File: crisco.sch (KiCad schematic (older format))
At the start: 43 parts, among them J1 LED, J2 OLED, U1 ProMicro

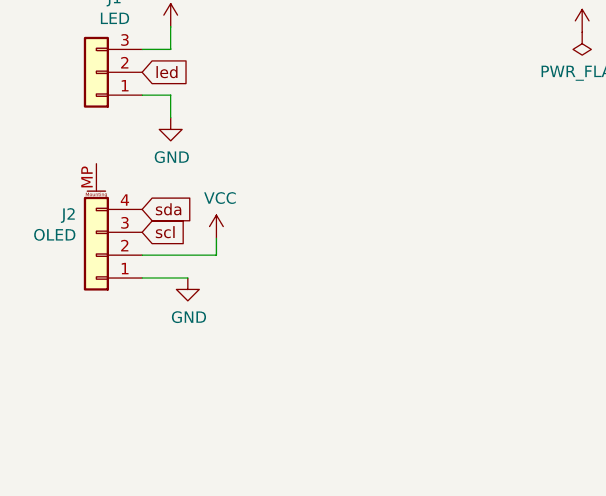
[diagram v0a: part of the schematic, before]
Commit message: added pullup resistors, bom, and instructions
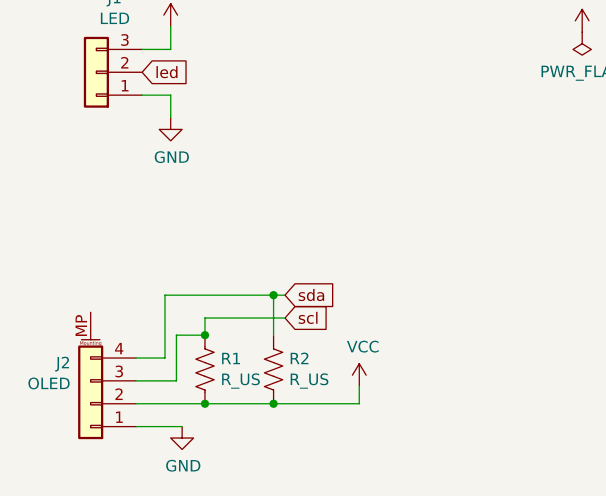
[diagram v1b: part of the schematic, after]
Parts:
- added R1, R2: R_US, Resistor_THT:R_Axial_DIN0204_L3.6mm_D1.6mm_P5.08mm_Horizontal, symbol Device:R_US
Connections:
- net VCC: now also R1.2, R2.2
- net scl: now also R1.1
- net sda: now also R2.1
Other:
- moved on the sheet: J2
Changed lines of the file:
@@
 L Connector_Generic_MountingPin:Conn_01x04_MountingPin J2
 U 1 1 61CC6089
-P 1975 4600
-F 0 "J2" H 2063 4422 50  0000 L CNN
-F 1 "OLED" H 2063 4513 50  0000 L CNN
-F 2 "Connector_PinHeader_2.54mm:PinHeader_1x04_P2.54mm_Vertical" H 1975 4600 50  0001 C CNN
-F 3 "~" H 1975 4600 50  0001 C CNN
-	1    1975 4600
+P 1950 5250
+F 0 "J2" H 2038 5072 50  0000 L CNN
+F 1 "OLED" H 2038 5163 50  0000 L CNN
+F 2 "Connector_PinHeader_2.54mm:PinHeader_1x04_P2.54mm_Vertical" H 1950 5250 50  0001 C CNN
+F 3 "~" H 1950 5250 50  0001 C CNN
+	1    1950 5250
 	-1   0    0    1
 $EndComp
@@
 L power:VCC #PWR0109
 U 1 1 61CCE8B0
-P 2500 4525
-F 0 "#PWR0109" H 2500 4375 50  0001 C CNN
-F 1 "VCC" H 2517 4698 50  0000 C CNN
-F 2 "" H 2500 4525 50  0001 C CNN
-F 3 "" H 2500 4525 50  0001 C CNN
-	1    2500 4525
+P 3125 5175
+F 0 "#PWR0109" H 3125 5025 50  0001 C CNN
+F 1 "VCC" H 3142 5348 50  0000 C CNN
+F 2 "" H 3125 5175 50  0001 C CNN
+F 3 "" H 3125 5175 50  0001 C CNN
+	1    3125 5175
 	1    0    0    -1
 $EndComp
@@
 L power:GND #PWR0110
 U 1 1 61CD2B6D
-P 2375 4700
-F 0 "#PWR0110" H 2375 4450 50  0001 C CNN
-F 1 "GND" H 2380 4527 50  0000 C CNN
-F 2 "" H 2375 4700 50  0001 C CNN
-F 3 "" H 2375 4700 50  0001 C CNN
-	1    2375 4700
+P 2350 5350
+F 0 "#PWR0110" H 2350 5100 50  0001 C CNN
+F 1 "GND" H 2355 5177 50  0000 C CNN
+F 2 "" H 2350 5350 50  0001 C CNN
+F 3 "" H 2350 5350 50  0001 C CNN
+	1    2350 5350
 	1    0    0    -1
 $EndComp
-Text GLabel 2175 4500 2    50   Input ~ 0
+Text GLabel 2800 4875 2    50   Input ~ 0
 scl
-Text GLabel 2175 4400 2    50   Input ~ 0
+Text GLabel 2800 4775 2    50   Input ~ 0
 sda
 Wire Wire Line
-	2175 4600 2500 4600
+	3125 5250 3125 5175
 Wire Wire Line
-	2500 4600 2500 4525
+	2150 5350 2350 5350
+NoConn ~ 3650 2200
+$Comp
+L Device:R_US R1
+U 1 1 61D4AEF9
+P 2450 5100
+F 0 "R1" H 2518 5146 50  0000 L CNN
+F 1 "R_US" H 2518 5055 50  0000 L CNN
+F 2 "Resistor_THT:R_Axial_DIN0204_L3.6mm_D1.6mm_P5.08mm_Horizontal" V 2490 5090 50  0001 C CNN
+F 3 "~" H 2450 5100 50  0001 C CNN
+	1    2450 5100
+	1    0    0    -1
+$EndComp
+$Comp
+L Device:R_US R2
+U 1 1 61D4BA80
+P 2750 5100
+F 0 "R2" H 2818 5146 50  0000 L CNN
+F 1 "R_US" H 2818 5055 50  0000 L CNN
+F 2 "Resistor_THT:R_Axial_DIN0204_L3.6mm_D1.6mm_P5.08mm_Horizontal" V 2790 5090 50  0001 C CNN
+F 3 "~" H 2750 5100 50  0001 C CNN
+	1    2750 5100
+	1    0    0    -1
+$EndComp
 Wire Wire Line
-	2175 4700 2375 4700
-NoConn ~ 3650 2200
+	2750 5250 3125 5250
+Wire Wire Line
+	2750 5250 2450 5250
+Connection ~ 2750 5250
+Wire Wire Line
+	2450 5250 2150 5250
+Connection ~ 2450 5250
+Wire Wire Line
+	2325 5150 2150 5150
+Wire Wire Line
+	2275 5050 2275 4775
+Wire Wire Line
+	2275 4775 2750 4775
+Wire Wire Line
+	2325 4950 2450 4950
+Wire Wire Line
+	2450 4950 2450 4875
+Wire Wire Line
+	2450 4875 2800 4875
+Wire Wire Line
+	2325 4950 2325 5150
+Connection ~ 2450 4950
+Wire Wire Line
+	2750 4775 2750 4950
+Connection ~ 2750 4775
+Wire Wire Line
+	2750 4775 2800 4775
+Wire Wire Line
+	2150 5050 2275 5050
 $EndSCHEMATC

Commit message: update gerber
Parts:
- removed R1, R2: R_US, Resistor_THT:R_Axial_DIN0204_L3.6mm_D1.6mm_P5.08mm_Horizontal, symbol Device:R_US
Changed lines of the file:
@@
 L power:VCC #PWR0109
 U 1 1 61CCE8B0
-P 3125 5175
-F 0 "#PWR0109" H 3125 5025 50  0001 C CNN
-F 1 "VCC" H 3142 5348 50  0000 C CNN
-F 2 "" H 3125 5175 50  0001 C CNN
-F 3 "" H 3125 5175 50  0001 C CNN
-	1    3125 5175
+P 2625 5175
+F 0 "#PWR0109" H 2625 5025 50  0001 C CNN
+F 1 "VCC" H 2642 5348 50  0000 C CNN
+F 2 "" H 2625 5175 50  0001 C CNN
+F 3 "" H 2625 5175 50  0001 C CNN
+	1    2625 5175
 	1    0    0    -1
 $EndComp
@@
 	1    0    0    -1
 $EndComp
-Text GLabel 2800 4875 2    50   Input ~ 0
+Text GLabel 2150 5150 2    50   Input ~ 0
 scl
-Text GLabel 2800 4775 2    50   Input ~ 0
+Text GLabel 2150 5050 2    50   Input ~ 0
 sda
 Wire Wire Line
-	3125 5250 3125 5175
+	2625 5250 2625 5175
 Wire Wire Line
 	2150 5350 2350 5350
 NoConn ~ 3650 2200
-$Comp
-L Device:R_US R1
-U 1 1 61D4AEF9
-P 2450 5100
-F 0 "R1" H 2518 5146 50  0000 L CNN
-F 1 "R_US" H 2518 5055 50  0000 L CNN
-F 2 "Resistor_THT:R_Axial_DIN0204_L3.6mm_D1.6mm_P5.08mm_Horizontal" V 2490 5090 50  0001 C CNN
-F 3 "~" H 2450 5100 50  0001 C CNN
-	1    2450 5100
-	1    0    0    -1
-$EndComp
-$Comp
-L Device:R_US R2
-U 1 1 61D4BA80
-P 2750 5100
-F 0 "R2" H 2818 5146 50  0000 L CNN
-F 1 "R_US" H 2818 5055 50  0000 L CNN
-F 2 "Resistor_THT:R_Axial_DIN0204_L3.6mm_D1.6mm_P5.08mm_Horizontal" V 2790 5090 50  0001 C CNN
-F 3 "~" H 2750 5100 50  0001 C CNN
-	1    2750 5100
-	1    0    0    -1
-$EndComp
 Wire Wire Line
-	2750 5250 3125 5250
-Wire Wire Line
-	2750 5250 2450 5250
-Connection ~ 2750 5250
-Wire Wire Line
-	2450 5250 2150 5250
-Connection ~ 2450 5250
-Wire Wire Line
-	2325 5150 2150 5150
-Wire Wire Line
-	2275 5050 2275 4775
-Wire Wire Line
-	2275 4775 2750 4775
-Wire Wire Line
-	2325 4950 2450 4950
-Wire Wire Line
-	2450 4950 2450 4875
-Wire Wire Line
-	2450 4875 2800 4875
-Wire Wire Line
-	2325 4950 2325 5150
-Connection ~ 2450 4950
-Wire Wire Line
-	2750 4775 2750 4950
-Connection ~ 2750 4775
-Wire Wire Line
-	2750 4775 2800 4775
-Wire Wire Line
-	2150 5050 2275 5050
+	2150 5250 2625 5250
 $EndSCHEMATC

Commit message: reset switch
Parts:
- added SW1: SW_Push, Button_Switch_SMD:SW_SPST_B3U-1000P, symbol Switch:SW_Push
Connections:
- net GND: now also SW1.2
- net rst: now reaches U1.22 (RST)
- net rst: now also SW1.1
- no-connect marks 45 -> 44
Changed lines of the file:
@@
 Wire Wire Line
 	2150 5350 2350 5350
-NoConn ~ 3650 2200
 Wire Wire Line
 	2150 5250 2625 5250
+Text GLabel 3650 2200 2    50   Input ~ 0
+rst
+$Comp
+L Switch:SW_Push SW1
+U 1 1 61D5D662
+P 3175 3875
+F 0 "SW1" H 3175 4160 50  0000 C CNN
+F 1 "SW_Push" H 3175 4069 50  0000 C CNN
+F 2 "Button_Switch_SMD:SW_SPST_B3U-1000P" H 3175 4075 50  0001 C CNN
+F 3 "~" H 3175 4075 50  0001 C CNN
+	1    3175 3875
+	1    0    0    -1
+$EndComp
+Text GLabel 2975 3875 0    50   Input ~ 0
+rst
+$Comp
+L power:GND #PWR0106
+U 1 1 61D6114F
+P 3375 3875
+F 0 "#PWR0106" H 3375 3625 50  0001 C CNN
+F 1 "GND" H 3380 3702 50  0000 C CNN
+F 2 "" H 3375 3875 50  0001 C CNN
+F 3 "" H 3375 3875 50  0001 C CNN
+	1    3375 3875
+	1    0    0    -1
+$EndComp
 $EndSCHEMATC

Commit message: mx/alps hybrid version
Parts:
- MX1, MX10, MX11, MX12, MX13, MX14, MX15, MX16, MX17, MX18, MX19, MX2, MX20, MX3, MX4, MX5, MX6, MX7, MX8, MX9: footprint MX_Alps_Hybrid:MXOnly-1U-NoLED -> MX_Alps_Hybrid:MX-1U-NoLED
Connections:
- net GND: now also J2.MP (MountPin)
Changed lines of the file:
@@
 F 0 "MX1" H 5036 2217 60  0000 C CNN
 F 1 "MX-1U" H 5036 2143 20  0000 C CNN
-F 2 "MX_Alps_Hybrid:MXOnly-1U-NoLED" H 4925 1975 60  0001 C CNN
+F 2 "MX_Alps_Hybrid:MX-1U-NoLED" H 4925 1975 60  0001 C CNN
 F 3 "" H 4925 1975 60  0001 C CNN
 	1    4950 2000
@@
 F 0 "MX2" H 5636 2217 60  0000 C CNN
 F 1 "MX-1U" H 5636 2143 20  0000 C CNN
-F 2 "MX_Alps_Hybrid:MXOnly-1U-NoLED" H 5525 1975 60  0001 C CNN
+F 2 "MX_Alps_Hybrid:MX-1U-NoLED" H 5525 1975 60  0001 C CNN
 F 3 "" H 5525 1975 60  0001 C CNN
 	1    5550 2000
@@
 F 0 "MX3" H 6236 2217 60  0000 C CNN
 F 1 "MX-1U" H 6236 2143 20  0000 C CNN
-F 2 "MX_Alps_Hybrid:MXOnly-1U-NoLED" H 6125 1975 60  0001 C CNN
+F 2 "MX_Alps_Hybrid:MX-1U-NoLED" H 6125 1975 60  0001 C CNN
 F 3 "" H 6125 1975 60  0001 C CNN
 	1    6150 2000
@@
 F 0 "MX11" H 5036 2967 60  0000 C CNN
 F 1 "MX-1U" H 5036 2893 20  0000 C CNN
-F 2 "MX_Alps_Hybrid:MXOnly-1U-NoLED" H 4925 2725 60  0001 C CNN
+F 2 "MX_Alps_Hybrid:MX-1U-NoLED" H 4925 2725 60  0001 C CNN
 F 3 "" H 4925 2725 60  0001 C CNN
 	1    4950 2750
@@
 F 0 "MX12" H 5636 2967 60  0000 C CNN
 F 1 "MX-1U" H 5636 2893 20  0000 C CNN
-F 2 "MX_Alps_Hybrid:MXOnly-1U-NoLED" H 5525 2725 60  0001 C CNN
+F 2 "MX_Alps_Hybrid:MX-1U-NoLED" H 5525 2725 60  0001 C CNN
 F 3 "" H 5525 2725 60  0001 C CNN
 	1    5550 2750
@@
 F 0 "MX13" H 6236 2967 60  0000 C CNN
 F 1 "MX-1U" H 6236 2893 20  0000 C CNN
-F 2 "MX_Alps_Hybrid:MXOnly-1U-NoLED" H 6125 2725 60  0001 C CNN
+F 2 "MX_Alps_Hybrid:MX-1U-NoLED" H 6125 2725 60  0001 C CNN
 F 3 "" H 6125 2725 60  0001 C CNN
 	1    6150 2750
@@
 F 0 "MX4" H 6836 2217 60  0000 C CNN
 F 1 "MX-1U" H 6836 2143 20  0000 C CNN
-F 2 "MX_Alps_Hybrid:MXOnly-1U-NoLED" H 6725 1975 60  0001 C CNN
+F 2 "MX_Alps_Hybrid:MX-1U-NoLED" H 6725 1975 60  0001 C CNN
 F 3 "" H 6725 1975 60  0001 C CNN
 	1    6750 2000
@@
 F 0 "MX14" H 6836 2967 60  0000 C CNN
 F 1 "MX-1U" H 6836 2893 20  0000 C CNN
-F 2 "MX_Alps_Hybrid:MXOnly-1U-NoLED" H 6725 2725 60  0001 C CNN
+F 2 "MX_Alps_Hybrid:MX-1U-NoLED" H 6725 2725 60  0001 C CNN
 F 3 "" H 6725 2725 60  0001 C CNN
 	1    6750 2750
@@
 F 0 "MX5" H 7436 2217 60  0000 C CNN
 F 1 "MX-1U" H 7436 2143 20  0000 C CNN
-F 2 "MX_Alps_Hybrid:MXOnly-1U-NoLED" H 7325 1975 60  0001 C CNN
+F 2 "MX_Alps_Hybrid:MX-1U-NoLED" H 7325 1975 60  0001 C CNN
 F 3 "" H 7325 1975 60  0001 C CNN
 	1    7350 2000
@@
 F 0 "MX15" H 7436 2967 60  0000 C CNN
 F 1 "MX-1U" H 7436 2893 20  0000 C CNN
-F 2 "MX_Alps_Hybrid:MXOnly-1U-NoLED" H 7325 2725 60  0001 C CNN
+F 2 "MX_Alps_Hybrid:MX-1U-NoLED" H 7325 2725 60  0001 C CNN
 F 3 "" H 7325 2725 60  0001 C CNN
 	1    7350 2750
@@
 F 0 "MX6" H 8036 2217 60  0000 C CNN
 F 1 "MX-1U" H 8036 2143 20  0000 C CNN
-F 2 "MX_Alps_Hybrid:MXOnly-1U-NoLED" H 7925 1975 60  0001 C CNN
+F 2 "MX_Alps_Hybrid:MX-1U-NoLED" H 7925 1975 60  0001 C CNN
 F 3 "" H 7925 1975 60  0001 C CNN
 	1    7950 2000
@@
 F 0 "MX16" H 8036 2967 60  0000 C CNN
 F 1 "MX-1U" H 8036 2893 20  0000 C CNN
-F 2 "MX_Alps_Hybrid:MXOnly-1U-NoLED" H 7925 2725 60  0001 C CNN
+F 2 "MX_Alps_Hybrid:MX-1U-NoLED" H 7925 2725 60  0001 C CNN
 F 3 "" H 7925 2725 60  0001 C CNN
 	1    7950 2750
@@
 F 0 "MX7" H 8636 2217 60  0000 C CNN
 F 1 "MX-1U" H 8636 2143 20  0000 C CNN
-F 2 "MX_Alps_Hybrid:MXOnly-1U-NoLED" H 8525 1975 60  0001 C CNN
+F 2 "MX_Alps_Hybrid:MX-1U-NoLED" H 8525 1975 60  0001 C CNN
 F 3 "" H 8525 1975 60  0001 C CNN
 	1    8550 2000
@@
 F 0 "MX17" H 8636 2967 60  0000 C CNN
 F 1 "MX-1U" H 8636 2893 20  0000 C CNN
-F 2 "MX_Alps_Hybrid:MXOnly-1U-NoLED" H 8525 2725 60  0001 C CNN
+F 2 "MX_Alps_Hybrid:MX-1U-NoLED" H 8525 2725 60  0001 C CNN
 F 3 "" H 8525 2725 60  0001 C CNN
 	1    8550 2750
@@
 F 0 "MX8" H 9236 2217 60  0000 C CNN
 F 1 "MX-1U" H 9236 2143 20  0000 C CNN
-F 2 "MX_Alps_Hybrid:MXOnly-1U-NoLED" H 9125 1975 60  0001 C CNN
+F 2 "MX_Alps_Hybrid:MX-1U-NoLED" H 9125 1975 60  0001 C CNN
 F 3 "" H 9125 1975 60  0001 C CNN
 	1    9150 2000
@@
 F 0 "MX18" H 9236 2967 60  0000 C CNN
 F 1 "MX-1U" H 9236 2893 20  0000 C CNN
-F 2 "MX_Alps_Hybrid:MXOnly-1U-NoLED" H 9125 2725 60  0001 C CNN
+F 2 "MX_Alps_Hybrid:MX-1U-NoLED" H 9125 2725 60  0001 C CNN
 F 3 "" H 9125 2725 60  0001 C CNN
 	1    9150 2750
@@
 F 0 "MX9" H 9836 2217 60  0000 C CNN
 F 1 "MX-1U" H 9836 2143 20  0000 C CNN
-F 2 "MX_Alps_Hybrid:MXOnly-1U-NoLED" H 9725 1975 60  0001 C CNN
+F 2 "MX_Alps_Hybrid:MX-1U-NoLED" H 9725 1975 60  0001 C CNN
 F 3 "" H 9725 1975 60  0001 C CNN
 	1    9750 2000
@@
 F 0 "MX19" H 9836 2967 60  0000 C CNN
 F 1 "MX-1U" H 9836 2893 20  0000 C CNN
-F 2 "MX_Alps_Hybrid:MXOnly-1U-NoLED" H 9725 2725 60  0001 C CNN
+F 2 "MX_Alps_Hybrid:MX-1U-NoLED" H 9725 2725 60  0001 C CNN
 F 3 "" H 9725 2725 60  0001 C CNN
 	1    9750 2750
@@
 F 0 "MX10" H 10436 2217 60  0000 C CNN
 F 1 "MX-1U" H 10436 2143 20  0000 C CNN
-F 2 "MX_Alps_Hybrid:MXOnly-1U-NoLED" H 10325 1975 60  0001 C CNN
+F 2 "MX_Alps_Hybrid:MX-1U-NoLED" H 10325 1975 60  0001 C CNN
 F 3 "" H 10325 1975 60  0001 C CNN
 	1    10350 2000
@@
 F 0 "MX20" H 10436 2967 60  0000 C CNN
 F 1 "MX-1U" H 10436 2893 20  0000 C CNN
-F 2 "MX_Alps_Hybrid:MXOnly-1U-NoLED" H 10325 2725 60  0001 C CNN
+F 2 "MX_Alps_Hybrid:MX-1U-NoLED" H 10325 2725 60  0001 C CNN
 F 3 "" H 10325 2725 60  0001 C CNN
 	1    10350 2750
@@
 	1    0    0    -1
 $EndComp
+$Comp
+L power:GND #PWR0111
+U 1 1 61D60F29
+P 1950 4850
+F 0 "#PWR0111" H 1950 4600 50  0001 C CNN
+F 1 "GND" H 1955 4677 50  0000 C CNN
+F 2 "" H 1950 4850 50  0001 C CNN
+F 3 "" H 1950 4850 50  0001 C CNN
+	1    1950 4850
+	-1   0    0    1
+$EndComp
 $EndSCHEMATC

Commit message: choc hybrid
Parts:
- MX1, MX10, MX11, MX12, MX13, MX14, MX15, MX16, MX17, MX18, MX19, MX2, MX20, MX3, MX4, MX5, MX6, MX7, MX8, MX9: footprint MX_Alps_Hybrid:MX-1U-NoLED -> MX_Alps_Hybrid:MX-Choc-1U-NoLED
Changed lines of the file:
@@
 F 0 "MX1" H 5036 2217 60  0000 C CNN
 F 1 "MX-1U" H 5036 2143 20  0000 C CNN
-F 2 "MX_Alps_Hybrid:MX-1U-NoLED" H 4925 1975 60  0001 C CNN
+F 2 "MX_Alps_Hybrid:MX-Choc-1U-NoLED" H 4925 1975 60  0001 C CNN
 F 3 "" H 4925 1975 60  0001 C CNN
 	1    4950 2000
@@
 F 0 "MX2" H 5636 2217 60  0000 C CNN
 F 1 "MX-1U" H 5636 2143 20  0000 C CNN
-F 2 "MX_Alps_Hybrid:MX-1U-NoLED" H 5525 1975 60  0001 C CNN
+F 2 "MX_Alps_Hybrid:MX-Choc-1U-NoLED" H 5525 1975 60  0001 C CNN
 F 3 "" H 5525 1975 60  0001 C CNN
 	1    5550 2000
@@
 F 0 "MX3" H 6236 2217 60  0000 C CNN
 F 1 "MX-1U" H 6236 2143 20  0000 C CNN
-F 2 "MX_Alps_Hybrid:MX-1U-NoLED" H 6125 1975 60  0001 C CNN
+F 2 "MX_Alps_Hybrid:MX-Choc-1U-NoLED" H 6125 1975 60  0001 C CNN
 F 3 "" H 6125 1975 60  0001 C CNN
 	1    6150 2000
@@
 F 0 "MX11" H 5036 2967 60  0000 C CNN
 F 1 "MX-1U" H 5036 2893 20  0000 C CNN
-F 2 "MX_Alps_Hybrid:MX-1U-NoLED" H 4925 2725 60  0001 C CNN
+F 2 "MX_Alps_Hybrid:MX-Choc-1U-NoLED" H 4925 2725 60  0001 C CNN
 F 3 "" H 4925 2725 60  0001 C CNN
 	1    4950 2750
@@
 F 0 "MX12" H 5636 2967 60  0000 C CNN
 F 1 "MX-1U" H 5636 2893 20  0000 C CNN
-F 2 "MX_Alps_Hybrid:MX-1U-NoLED" H 5525 2725 60  0001 C CNN
+F 2 "MX_Alps_Hybrid:MX-Choc-1U-NoLED" H 5525 2725 60  0001 C CNN
 F 3 "" H 5525 2725 60  0001 C CNN
 	1    5550 2750
@@
 F 0 "MX13" H 6236 2967 60  0000 C CNN
 F 1 "MX-1U" H 6236 2893 20  0000 C CNN
-F 2 "MX_Alps_Hybrid:MX-1U-NoLED" H 6125 2725 60  0001 C CNN
+F 2 "MX_Alps_Hybrid:MX-Choc-1U-NoLED" H 6125 2725 60  0001 C CNN
 F 3 "" H 6125 2725 60  0001 C CNN
 	1    6150 2750
@@
 F 0 "MX4" H 6836 2217 60  0000 C CNN
 F 1 "MX-1U" H 6836 2143 20  0000 C CNN
-F 2 "MX_Alps_Hybrid:MX-1U-NoLED" H 6725 1975 60  0001 C CNN
+F 2 "MX_Alps_Hybrid:MX-Choc-1U-NoLED" H 6725 1975 60  0001 C CNN
 F 3 "" H 6725 1975 60  0001 C CNN
 	1    6750 2000
@@
 F 0 "MX14" H 6836 2967 60  0000 C CNN
 F 1 "MX-1U" H 6836 2893 20  0000 C CNN
-F 2 "MX_Alps_Hybrid:MX-1U-NoLED" H 6725 2725 60  0001 C CNN
+F 2 "MX_Alps_Hybrid:MX-Choc-1U-NoLED" H 6725 2725 60  0001 C CNN
 F 3 "" H 6725 2725 60  0001 C CNN
 	1    6750 2750
@@
 F 0 "MX5" H 7436 2217 60  0000 C CNN
 F 1 "MX-1U" H 7436 2143 20  0000 C CNN
-F 2 "MX_Alps_Hybrid:MX-1U-NoLED" H 7325 1975 60  0001 C CNN
+F 2 "MX_Alps_Hybrid:MX-Choc-1U-NoLED" H 7325 1975 60  0001 C CNN
 F 3 "" H 7325 1975 60  0001 C CNN
 	1    7350 2000
@@
 F 0 "MX15" H 7436 2967 60  0000 C CNN
 F 1 "MX-1U" H 7436 2893 20  0000 C CNN
-F 2 "MX_Alps_Hybrid:MX-1U-NoLED" H 7325 2725 60  0001 C CNN
+F 2 "MX_Alps_Hybrid:MX-Choc-1U-NoLED" H 7325 2725 60  0001 C CNN
 F 3 "" H 7325 2725 60  0001 C CNN
 	1    7350 2750
@@
 F 0 "MX6" H 8036 2217 60  0000 C CNN
 F 1 "MX-1U" H 8036 2143 20  0000 C CNN
-F 2 "MX_Alps_Hybrid:MX-1U-NoLED" H 7925 1975 60  0001 C CNN
+F 2 "MX_Alps_Hybrid:MX-Choc-1U-NoLED" H 7925 1975 60  0001 C CNN
 F 3 "" H 7925 1975 60  0001 C CNN
 	1    7950 2000
@@
 F 0 "MX16" H 8036 2967 60  0000 C CNN
 F 1 "MX-1U" H 8036 2893 20  0000 C CNN
-F 2 "MX_Alps_Hybrid:MX-1U-NoLED" H 7925 2725 60  0001 C CNN
+F 2 "MX_Alps_Hybrid:MX-Choc-1U-NoLED" H 7925 2725 60  0001 C CNN
 F 3 "" H 7925 2725 60  0001 C CNN
 	1    7950 2750
@@
 F 0 "MX7" H 8636 2217 60  0000 C CNN
 F 1 "MX-1U" H 8636 2143 20  0000 C CNN
-F 2 "MX_Alps_Hybrid:MX-1U-NoLED" H 8525 1975 60  0001 C CNN
+F 2 "MX_Alps_Hybrid:MX-Choc-1U-NoLED" H 8525 1975 60  0001 C CNN
 F 3 "" H 8525 1975 60  0001 C CNN
 	1    8550 2000
@@
 F 0 "MX17" H 8636 2967 60  0000 C CNN
 F 1 "MX-1U" H 8636 2893 20  0000 C CNN
-F 2 "MX_Alps_Hybrid:MX-1U-NoLED" H 8525 2725 60  0001 C CNN
+F 2 "MX_Alps_Hybrid:MX-Choc-1U-NoLED" H 8525 2725 60  0001 C CNN
 F 3 "" H 8525 2725 60  0001 C CNN
 	1    8550 2750
@@
 F 0 "MX8" H 9236 2217 60  0000 C CNN
 F 1 "MX-1U" H 9236 2143 20  0000 C CNN
-F 2 "MX_Alps_Hybrid:MX-1U-NoLED" H 9125 1975 60  0001 C CNN
+F 2 "MX_Alps_Hybrid:MX-Choc-1U-NoLED" H 9125 1975 60  0001 C CNN
 F 3 "" H 9125 1975 60  0001 C CNN
 	1    9150 2000
@@
 F 0 "MX18" H 9236 2967 60  0000 C CNN
 F 1 "MX-1U" H 9236 2893 20  0000 C CNN
-F 2 "MX_Alps_Hybrid:MX-1U-NoLED" H 9125 2725 60  0001 C CNN
+F 2 "MX_Alps_Hybrid:MX-Choc-1U-NoLED" H 9125 2725 60  0001 C CNN
 F 3 "" H 9125 2725 60  0001 C CNN
 	1    9150 2750
@@
 F 0 "MX9" H 9836 2217 60  0000 C CNN
 F 1 "MX-1U" H 9836 2143 20  0000 C CNN
-F 2 "MX_Alps_Hybrid:MX-1U-NoLED" H 9725 1975 60  0001 C CNN
+F 2 "MX_Alps_Hybrid:MX-Choc-1U-NoLED" H 9725 1975 60  0001 C CNN
 F 3 "" H 9725 1975 60  0001 C CNN
 	1    9750 2000
@@
 F 0 "MX19" H 9836 2967 60  0000 C CNN
 F 1 "MX-1U" H 9836 2893 20  0000 C CNN
-F 2 "MX_Alps_Hybrid:MX-1U-NoLED" H 9725 2725 60  0001 C CNN
+F 2 "MX_Alps_Hybrid:MX-Choc-1U-NoLED" H 9725 2725 60  0001 C CNN
 F 3 "" H 9725 2725 60  0001 C CNN
 	1    9750 2750
@@
 F 0 "MX10" H 10436 2217 60  0000 C CNN
 F 1 "MX-1U" H 10436 2143 20  0000 C CNN
-F 2 "MX_Alps_Hybrid:MX-1U-NoLED" H 10325 1975 60  0001 C CNN
+F 2 "MX_Alps_Hybrid:MX-Choc-1U-NoLED" H 10325 1975 60  0001 C CNN
 F 3 "" H 10325 1975 60  0001 C CNN
 	1    10350 2000
@@
 F 0 "MX20" H 10436 2967 60  0000 C CNN
 F 1 "MX-1U" H 10436 2893 20  0000 C CNN
-F 2 "MX_Alps_Hybrid:MX-1U-NoLED" H 10325 2725 60  0001 C CNN
+F 2 "MX_Alps_Hybrid:MX-Choc-1U-NoLED" H 10325 2725 60  0001 C CNN
 F 3 "" H 10325 2725 60  0001 C CNN
 	1    10350 2750
